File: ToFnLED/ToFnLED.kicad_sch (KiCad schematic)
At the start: 10 parts, among them J1 Conn_01x04, J2 Conn_01x04, U1 PCA9632DP2_118, U2 VL53L1CXV0FY1

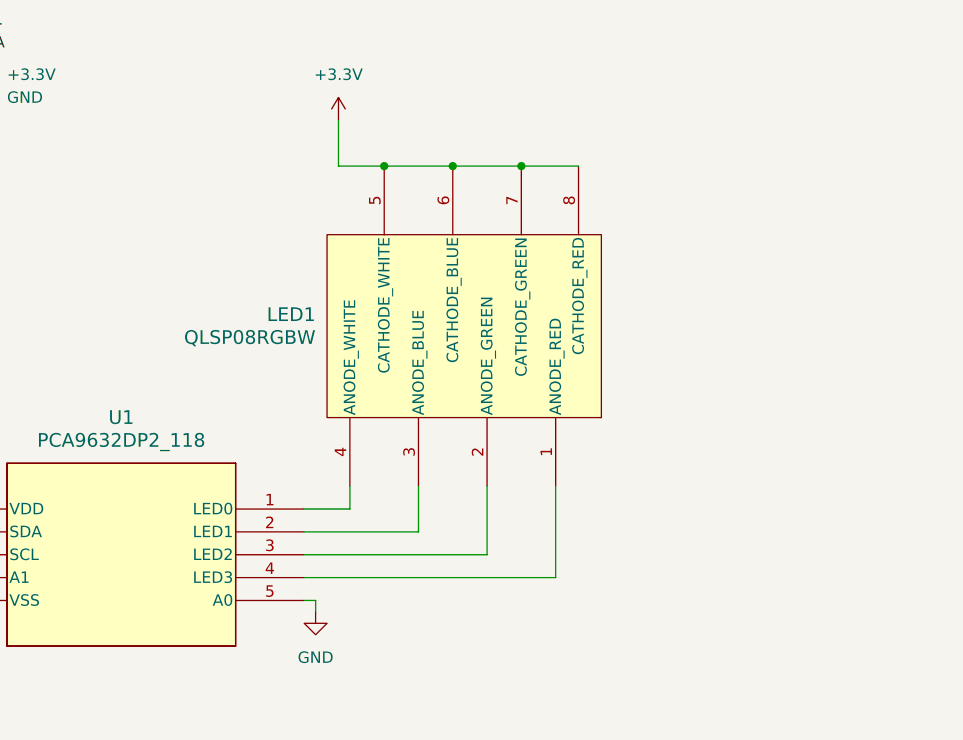
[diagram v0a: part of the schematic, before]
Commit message: Reversed LED connections
Reversed LED connections to match that of Someluckys version of the ToFnLED.
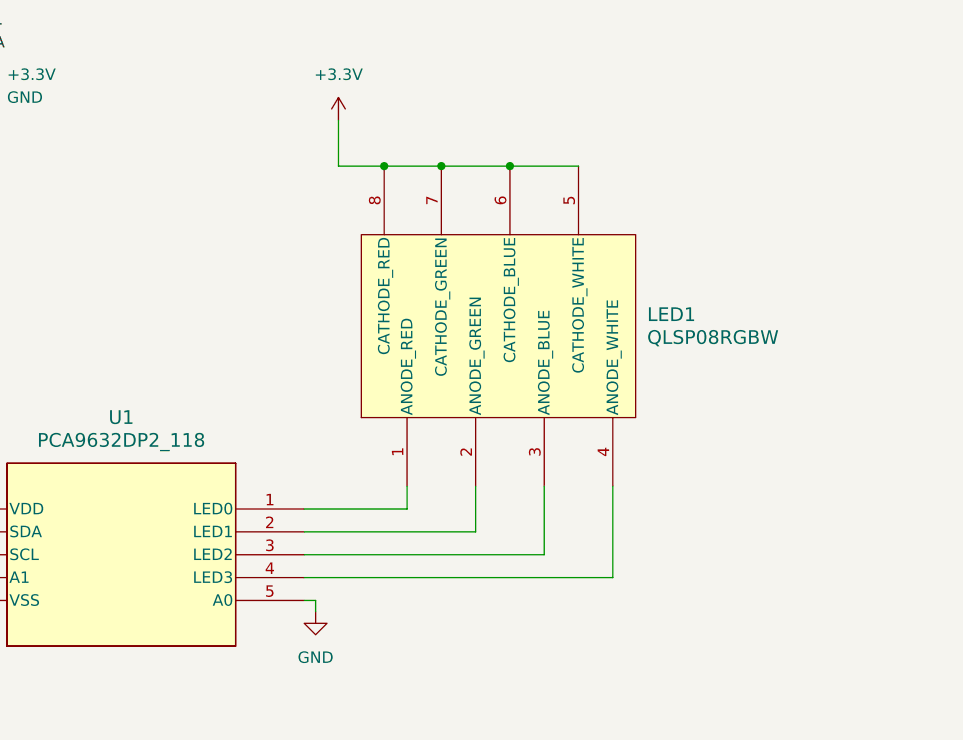
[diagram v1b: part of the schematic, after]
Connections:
- net at LED1.1 (ANODE_RED): now also U1.1 (LED0); no longer U1.4 (LED3)
- net at LED1.2 (ANODE_GREEN): now also U1.2 (LED1); no longer U1.3 (LED2)
- net at LED1.3 (ANODE_BLUE): now also U1.3 (LED2); no longer U1.2 (LED1)
- net at LED1.4 (ANODE_WHITE): now also U1.4 (LED3); no longer U1.1 (LED0)
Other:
- moved on the sheet: LED1
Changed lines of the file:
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@@
   (junction (at 133.35 161.29) (diameter 0) (color 0 0 0 0)
   )
-  (junction (at 129.54 74.93) (diameter 0) (color 0 0 0 0)
-  )
   (junction (at 198.12 71.12) (diameter 0) (color 0 0 0 0)
   )
+  (junction (at 128.27 74.93) (diameter 0) (color 0 0 0 0)
+  )
+  (junction (at 135.89 74.93) (diameter 0) (color 0 0 0 0)
+  )
   (junction (at 121.92 74.93) (diameter 0) (color 0 0 0 0)
   )
@@
   (junction (at 71.12 123.19) (diameter 0) (color 0 0 0 0)
   )
-  (junction (at 137.16 74.93) (diameter 0) (color 0 0 0 0)
-  )
   (junction (at 217.17 104.14) (diameter 0) (color 0 0 0 0)
   )
   (no_connect (at 207.01 82.55))
-  (wire (pts (xy 140.97 110.49) (xy 140.97 120.65))
-    (stroke (width 0) (type default))
-  )
-  (wire (pts (xy 140.97 120.65) (xy 113.03 120.65))
+  (wire (pts (xy 113.03 120.65) (xy 147.32 120.65))
     (stroke (width 0) (type default))
   )
@@
     (stroke (width 0) (type default))
   )
+  (wire (pts (xy 139.7 118.11) (xy 139.7 110.49))
+    (stroke (width 0) (type default))
+  )
   (wire (pts (xy 71.12 113.03) (xy 71.12 111.76))
     (stroke (width 0) (type default))
@@
     (stroke (width 0) (type default))
   )
+  (wire (pts (xy 147.32 120.65) (xy 147.32 110.49))
+    (stroke (width 0) (type default))
+  )
   (wire (pts (xy 133.35 161.29) (xy 133.35 162.56))
     (stroke (width 0) (type default))
   )
-  (wire (pts (xy 133.35 110.49) (xy 133.35 118.11))
-    (stroke (width 0) (type default))
-  )
   (wire (pts (xy 72.39 113.03) (xy 71.12 113.03))
     (stroke (width 0) (type default))
   )
-  (wire (pts (xy 125.73 110.49) (xy 125.73 115.57))
-    (stroke (width 0) (type default))
-  )
   (wire (pts (xy 198.12 95.25) (xy 207.01 95.25))
     (stroke (width 0) (type default))
   )
+  (wire (pts (xy 121.92 74.93) (xy 128.27 74.93))
+    (stroke (width 0) (type default))
+  )
   (wire (pts (xy 73.66 48.26) (xy 76.2 48.26))
     (stroke (width 0) (type default))
@@
     (stroke (width 0) (type default))
   )
-  (wire (pts (xy 137.16 74.93) (xy 143.51 74.93))
+  (wire (pts (xy 116.84 74.93) (xy 121.92 74.93))
     (stroke (width 0) (type default))
   )
@@
     (stroke (width 0) (type default))
   )
-  (wire (pts (xy 121.92 74.93) (xy 129.54 74.93))
-    (stroke (width 0) (type default))
-  )
-  (wire (pts (xy 116.84 74.93) (xy 121.92 74.93))
+  (wire (pts (xy 124.46 110.49) (xy 124.46 113.03))
+    (stroke (width 0) (type default))
+  )
+  (wire (pts (xy 128.27 74.93) (xy 135.89 74.93))
     (stroke (width 0) (type default))
   )
@@
     (stroke (width 0) (type default))
   )
+  (wire (pts (xy 132.08 115.57) (xy 132.08 110.49))
+    (stroke (width 0) (type default))
+  )
   (wire (pts (xy 198.12 71.12) (xy 198.12 83.82))
     (stroke (width 0) (type default))
@@
     (stroke (width 0) (type default))
   )
-  (wire (pts (xy 113.03 113.03) (xy 118.11 113.03))
-    (stroke (width 0) (type default))
-  )
-  (wire (pts (xy 133.35 118.11) (xy 113.03 118.11))
+  (wire (pts (xy 113.03 113.03) (xy 124.46 113.03))
+    (stroke (width 0) (type default))
+  )
+  (wire (pts (xy 135.89 74.93) (xy 143.51 74.93))
+    (stroke (width 0) (type default))
+  )
+  (wire (pts (xy 113.03 118.11) (xy 139.7 118.11))
     (stroke (width 0) (type default))
   )
@@
     (stroke (width 0) (type default))
   )
-  (wire (pts (xy 125.73 115.57) (xy 113.03 115.57))
+  (wire (pts (xy 113.03 115.57) (xy 132.08 115.57))
     (stroke (width 0) (type default))
   )
@@
   )
   (wire (pts (xy 198.12 91.44) (xy 198.12 95.25))
-    (stroke (width 0) (type default))
-  )
-  (wire (pts (xy 129.54 74.93) (xy 137.16 74.93))
-    (stroke (width 0) (type default))
-  )
-  (wire (pts (xy 118.11 110.49) (xy 118.11 113.03))
     (stroke (width 0) (type default))
   )
@@
     )
   )
-  (symbol (lib_id "2023-07-27_03-08-06:QLSP08RGBW") (at 146.05 102.87 270) (mirror x) (unit 1)
+  (symbol (lib_id "2023-07-27_03-08-06:QLSP08RGBW") (at 119.38 102.87 90) (unit 1)
     (in_bom yes) (on_board yes) (dnp no)
-    (property "Reference" "LED1" (at 114.3 91.44 90)
+    (property "Reference" "LED1" (at 151.13 91.44 90)
       (effects (font (size 1.524 1.524)) (justify right))
     )
-    (property "Value" "QLSP08RGBW" (at 114.3 93.98 90)
+    (property "Value" "QLSP08RGBW" (at 151.13 93.98 90)
       (effects (font (size 1.524 1.524)) (justify right))
     )
-    (property "Footprint" "footprints:QLSP08RGBW_QUE" (at 152.4 92.71 0)
+    (property "Footprint" "footprints:QLSP08RGBW_QUE" (at 113.03 92.71 0)
       (effects (font (size 1.27 1.27) italic) hide)
     )
-    (property "Datasheet" "QLSP08RGBW" (at 154.94 92.71 0)
+    (property "Datasheet" "QLSP08RGBW" (at 110.49 92.71 0)
       (effects (font (size 1.27 1.27) italic) hide)
     )
